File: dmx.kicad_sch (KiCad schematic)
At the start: 41 parts, among them J101 SJ2-25504B-SMT-TR, J102 CORTEX-DEBUG, J103 JAE_DX07S016JA1R1500, SW101 SW_Push, SW102 SW_Push, U101 LTC2851xDD, U102 ATSAMD51G, U103 AP2112K-3.3, Y101 32.768kHz

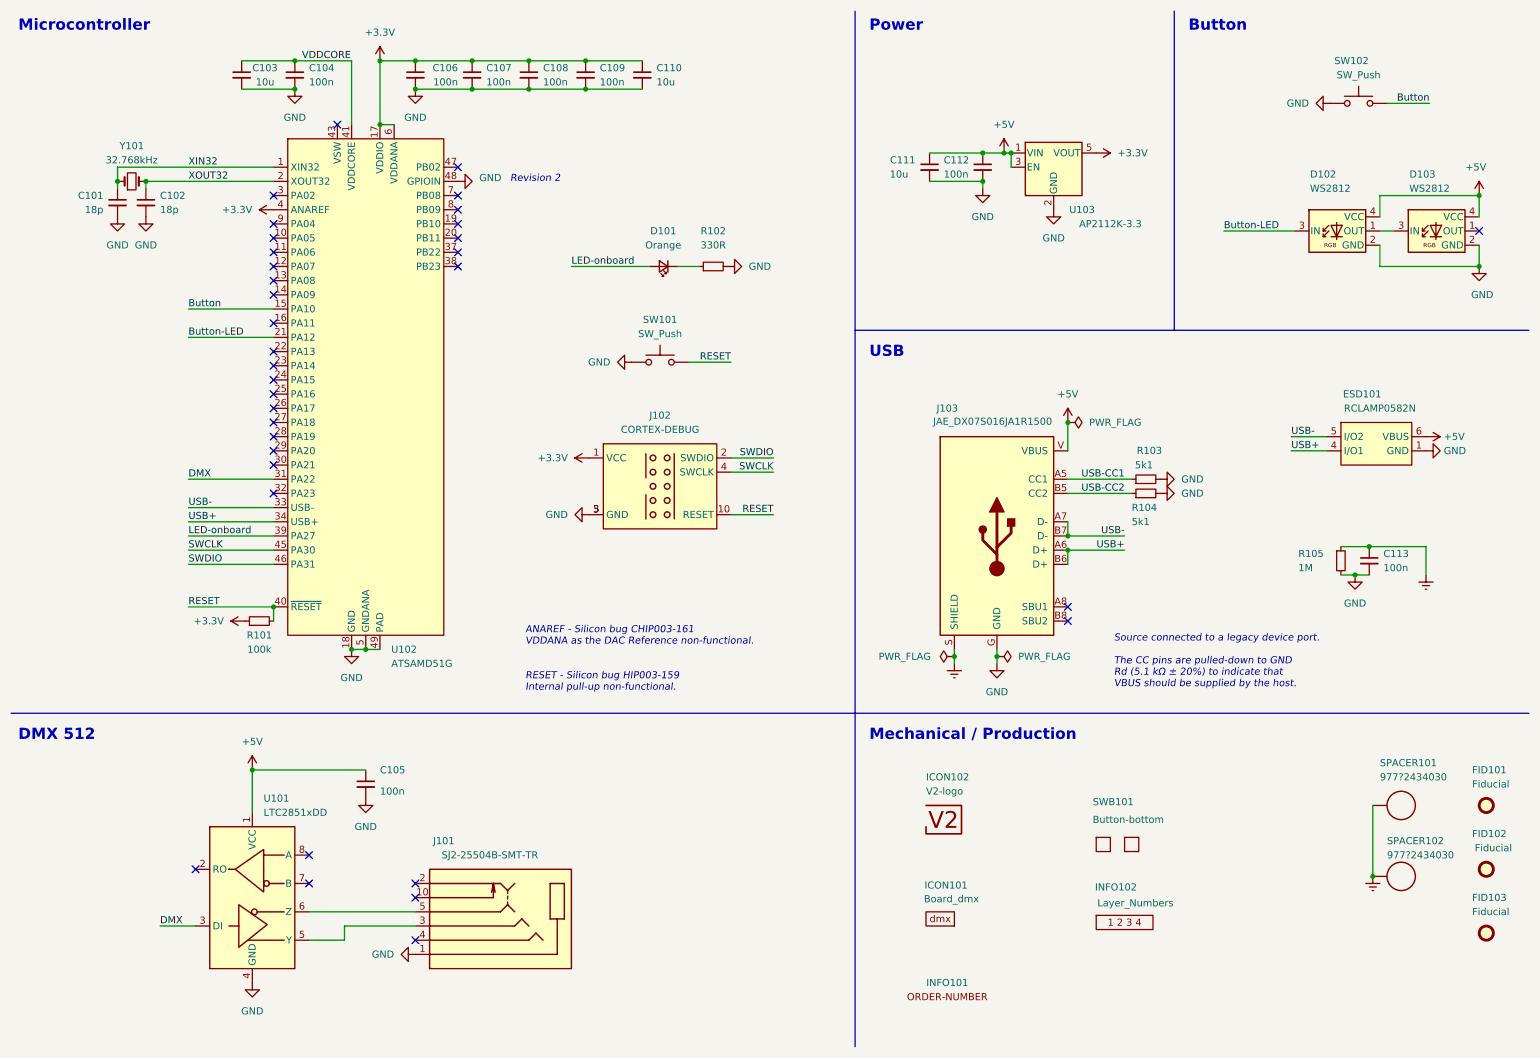
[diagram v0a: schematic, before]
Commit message: Update to KiCad 7.0
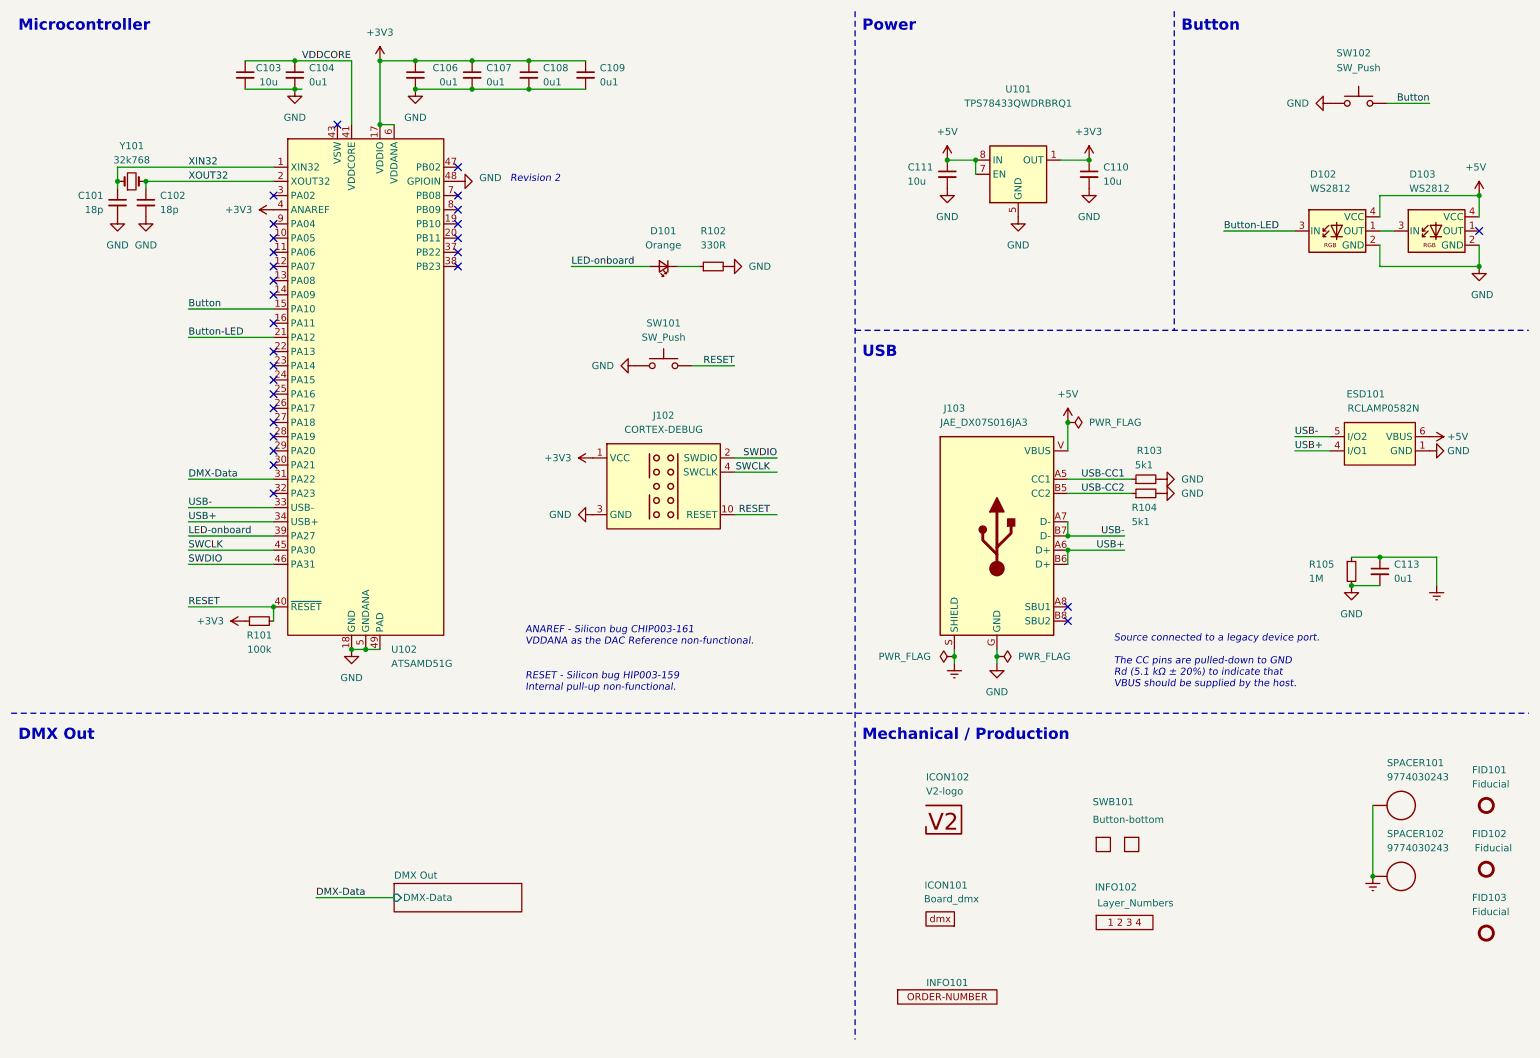
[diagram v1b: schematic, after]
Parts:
- removed C105, C112: 100n, Capacitor_SMD:C_0603_1608Metric, symbol Device:C_Small
- removed J101: SJ2-25504B-SMT-TR, V2_Connector_Audio:CUI_SJ2-25504B-SMT-TR, symbol V2_Connector_Audio:SJ2-25504B-SMT-TR
- removed U101: LTC2851xDD, Package_DFN_QFN:DFN-8-1EP_3x3mm_P0.5mm_EP1.66x2.38mm, symbol Interface_UART:LTC2851xDD
- removed U103: AP2112K-3.3, Package_TO_SOT_SMD:SOT-23-5, symbol Regulator_Linear:AP2112K-3.3
- added U101: TPS78433QWDRBRQ1, V2_Package_SON:VSON-8-1_3x3mm_P0.65_EP1.65x2.4mm, symbol V2_Regulator_Linear:TPS78433QWDRBRQ1
- C104, C106, C107, C108, C109, C113: value 100n -> 0u1
- FID101, FID102, FID103: now left out of the parts list
- J103: value JAE_DX07S016JA1R1500 -> JAE_DX07S016JA3; footprint V2_Connector_USB:JAE_DX07S016JA1R1500 -> V2_Connector_USB:JAE_DX07S016JA3; symbol V2_Connector_USB:JAE_DX07S016JA1R1500 -> V2_Connector_USB:JAE_DX07S016JA3
- SPACER101, SPACER102: value 977?2434030 -> 9774030243; symbol V2_Spacer_Wurth:977?2434030 -> V2_Spacer_Wurth:9774030243
- Y101: value 32.768kHz -> 32k768
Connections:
- net +5V: now also U101.7 (EN), U101.8 (IN)
- net GND: now also U101.5 (GND), U101.9 (GND)
- net +3.3V renamed +3V3
- net +3V3: now also U101.1 (OUT)
- net DMX renamed DMX-Data
- no-connect marks 35 -> 29
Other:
- added sheet DMX Out (DMXOut.kicad_sch)
- note added: "DMX Out"
- note removed: "DMX 512"
- moved on the sheet: C103, C110, C111, C113, ESD101, R105, SW101
